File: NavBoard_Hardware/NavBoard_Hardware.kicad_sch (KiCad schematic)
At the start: 45 parts, among them J1 6 Pin Molex Micro-Fit, U1 OKI-5V, U2 BHI160B, U3 ICM-20608-G, U4 OKI-3V3, U6 Raspberry_Pi

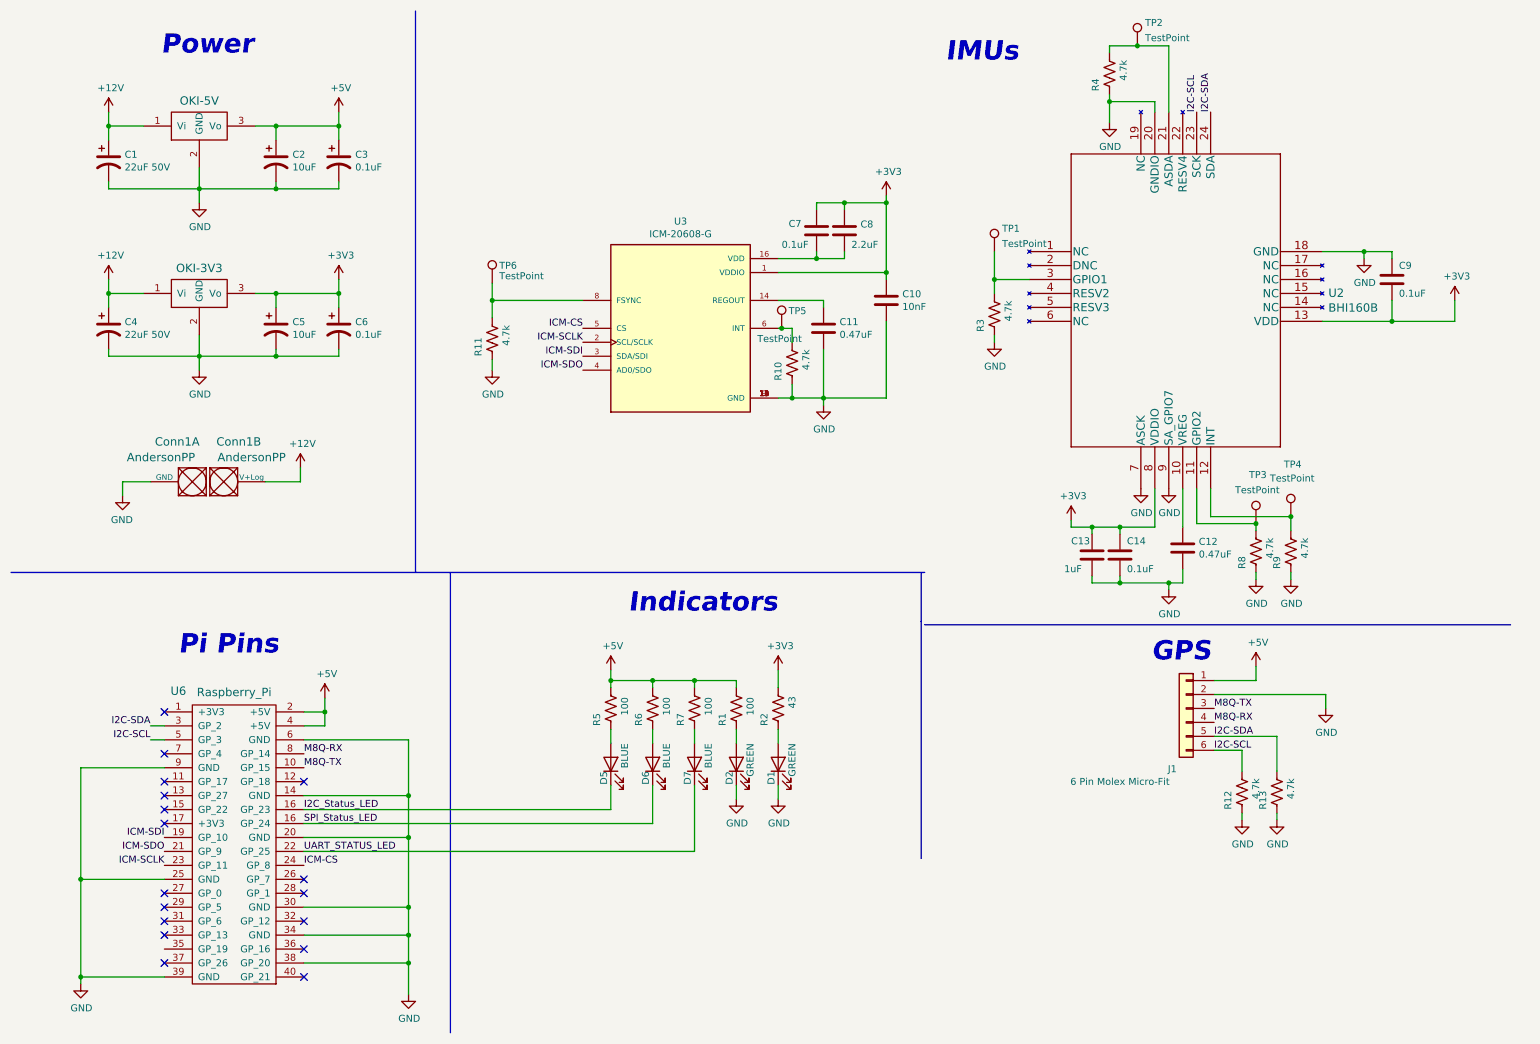
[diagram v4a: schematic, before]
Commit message: Component placement done (except LEDs), redesign of schematic pages, started documentation presentations
Leaving @katdun14 and @nvngx responsible for routing the status LEDs.
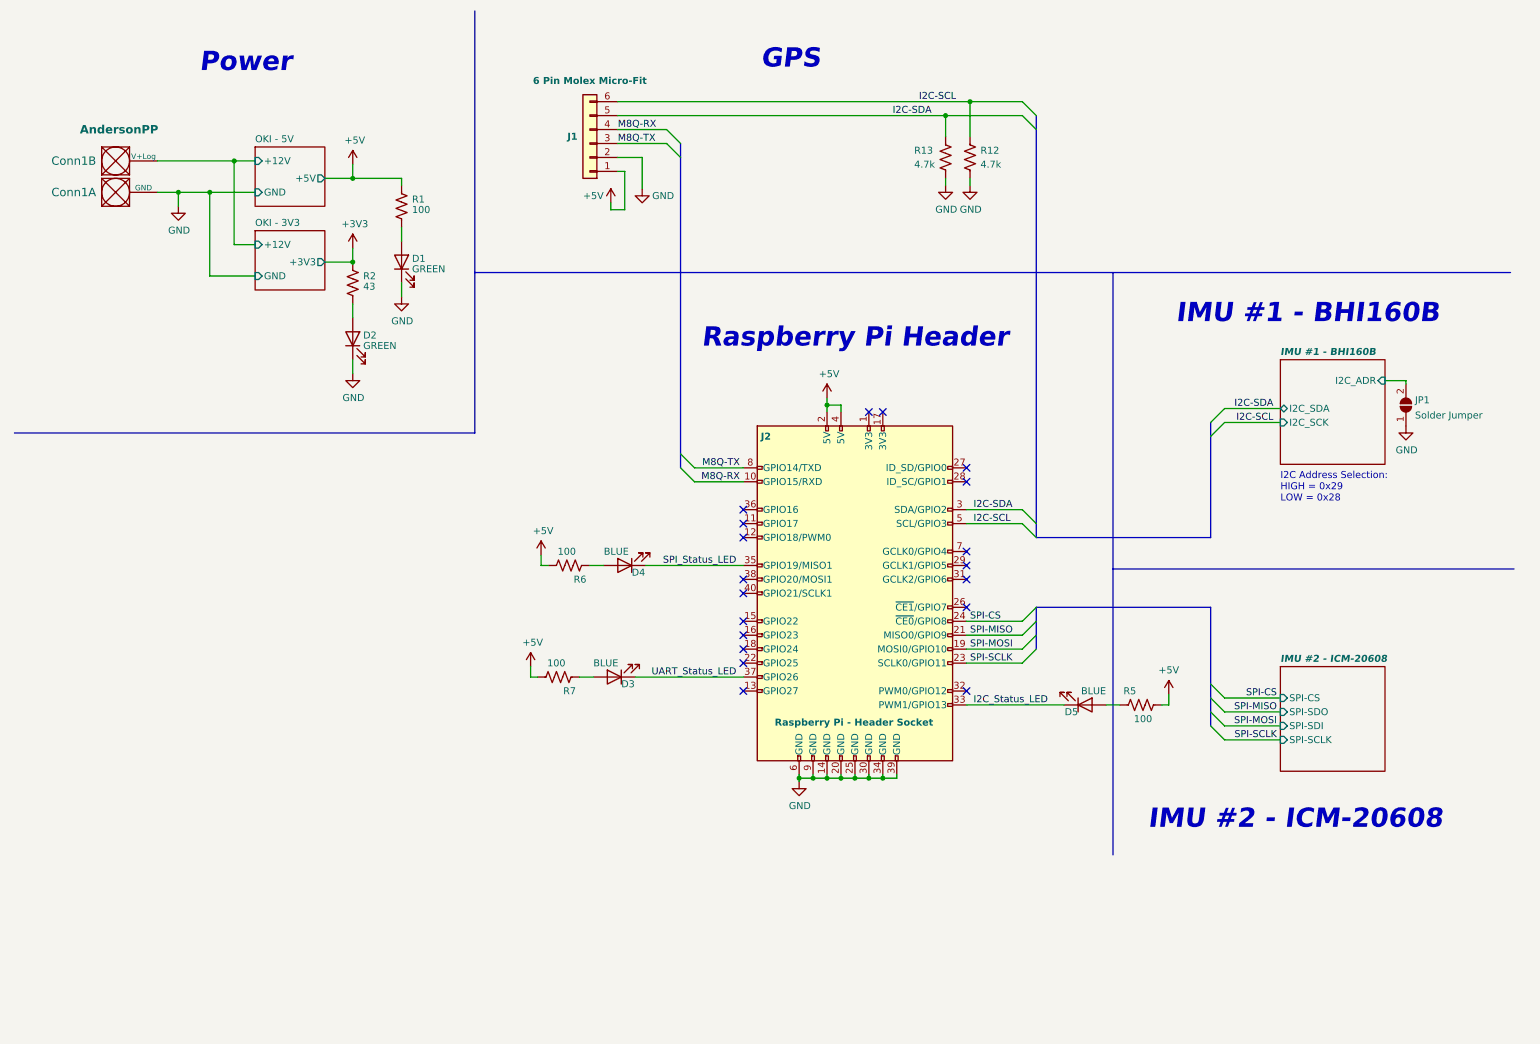
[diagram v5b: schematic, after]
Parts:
- removed C1, C4: 22uF 50V, Capacitor_THT:CP_Radial_D6.3mm_P2.50mm, symbol Device:C_Polarized_US
- removed C10: 10nF, Capacitor_SMD:C_0603_1608Metric_Pad1.08x0.95mm_HandSolder, symbol Device:C
- removed C11, C12: 0.47uF, Capacitor_SMD:C_0603_1608Metric_Pad1.08x0.95mm_HandSolder, symbol Device:C
- removed C13: 1uF, Capacitor_SMD:C_0603_1608Metric_Pad1.08x0.95mm_HandSolder, symbol Device:C
- removed C14, C7, C9: 0.1uF, Capacitor_SMD:C_0603_1608Metric_Pad1.08x0.95mm_HandSolder, symbol Device:C
- removed C2, C5: 10uF, Capacitor_SMD:C_0603_1608Metric_Pad1.08x0.95mm_HandSolder, symbol Device:C_Polarized_US
- removed C3, C6: 0.1uF, Capacitor_SMD:C_0603_1608Metric_Pad1.08x0.95mm_HandSolder, symbol Device:C_Polarized_US
- removed C8: 2.2uF, Capacitor_SMD:C_0603_1608Metric_Pad1.08x0.95mm_HandSolder, symbol Device:C
- removed R10, R11, R3, R4, R8, R9: 4.7k, Resistor_SMD:R_0603_1608Metric_Pad0.98x0.95mm_HandSolder, symbol Device:R_US
- removed TP1, TP2, TP3, TP4, TP5, TP6: TestPoint, TestPoint:TestPoint_Pad_D2.0mm, symbol Connector:TestPoint
- removed U1: OKI-5V, MRDT_Devices:OKI_Horizontal, symbol MRDT_Devices:OKI
- removed U2: BHI160B, LGA24_3X3X0P95_3_BOS, symbol MRDT_Sensors:BHI160B
- removed U3: ICM-20608-G, PQFN50P300X300X80-16N, symbol MRDT_Sensors:ICM-20608-G
- removed U4: OKI-3V3, MRDT_Devices:OKI_Horizontal, symbol MRDT_Devices:OKI
- removed U6: Raspberry_Pi, MRDT_Shields:RaspberryPi_THT_BOTTOM, symbol MRDT_Shields:Raspberry_Pi
- added J2: Raspberry Pi - Header Socket, MRDT_Shields:RaspberryPi_THT_BOTTOM, symbol Connector:Raspberry_Pi_2_3
- added JP1: Solder Jumper, Jumper:SolderJumper-2_P1.3mm_Open_RoundedPad1.0x1.5mm, symbol Jumper:SolderJumper_2_Open
- renumbered D2 to D1, D1 to D2, D7 to D3, D6 to D4
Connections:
- net +5V: now also J2.2 (5V), J2.4 (5V)
- net GND: now also J2.14 (GND), J2.20 (GND), J2.25 (GND), J2.30 (GND), J2.34 (GND), J2.39 (GND), J2.6 (GND), J2.9 (GND), JP1.1 (A)
- net I2C-SCL: now also J2.5 (SCL/GPIO3)
- net I2C-SDA: now also J2.3 (SDA/GPIO2)
- net I2C_Status_LED: now also J2.33 (PWM1/GPIO13)
- net M8Q-RX: now also J2.10 (GPIO15/RXD)
- net M8Q-TX: now also J2.8 (GPIO14/TXD)
- net SPI_Status_LED: now also J2.35 (GPIO19/MISO1)
- net +12V renamed OKI - 3V3/+12V
- net UART_STATUS_LED renamed UART_Status_LED
- net UART_Status_LED: now also J2.37 (GPIO26)
- new net IMU #1 - BHI160B/I2C_ADR: JP1.2 (B)
- new net SPI-CS: J2.24 (~{CE0}/GPIO8)
- new net SPI-MISO: J2.21 (MISO0/GPIO9)
- new net SPI-MOSI: J2.19 (MOSI0/GPIO10)
- new net SPI-SCLK: J2.23 (SCLK0/GPIO11)
- no-connect marks 17 -> 19
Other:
- added sheet IMU #1 - BHI160B (component_sheets\BHI160B.kicad_sch)
- added sheet IMU #2 - ICM-20608 (component_sheets\ICM-20608.kicad_sch)
- added sheet OKI - 3V3 (component_sheets\OKI-3V3.kicad_sch)
- added sheet OKI - 5V (component_sheets\OKI-5V.kicad_sch)
- note added: "I2C Address Selection: HIGH = 0x29 LOW = 0x28"
- note added: "IMU #1 - BHI160B"
- note added: "IMU #2 - ICM-20608"
- note added: "Raspberry Pi Header"
- note removed: "IMUs"
- note removed: "Indicators"
- note removed: "Pi Pins"
- moved on the sheet: Conn1A, Conn1B, D1, D2, D3, D4, D5, J1, R1, R12, R13, R2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

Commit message: Added ground vias for added isolation in substrate, worked on schematic review 1 powerpoint
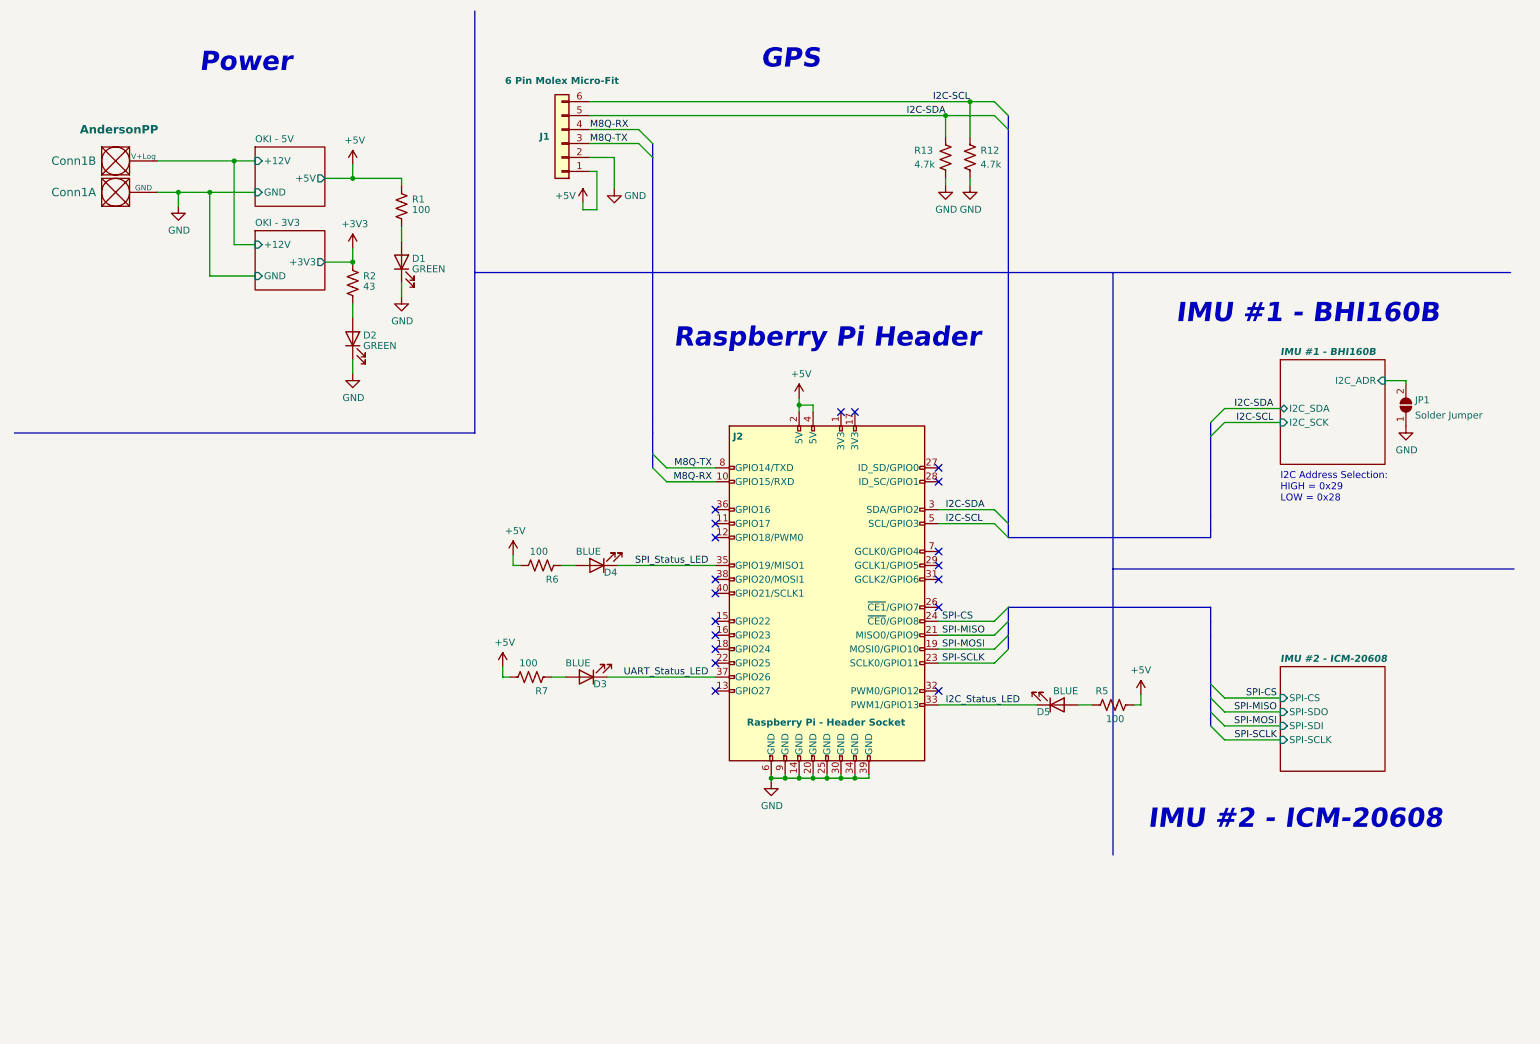
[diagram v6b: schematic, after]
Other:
- moved on the sheet: D3, D4, D5, J1, J2, R5, R6, R7

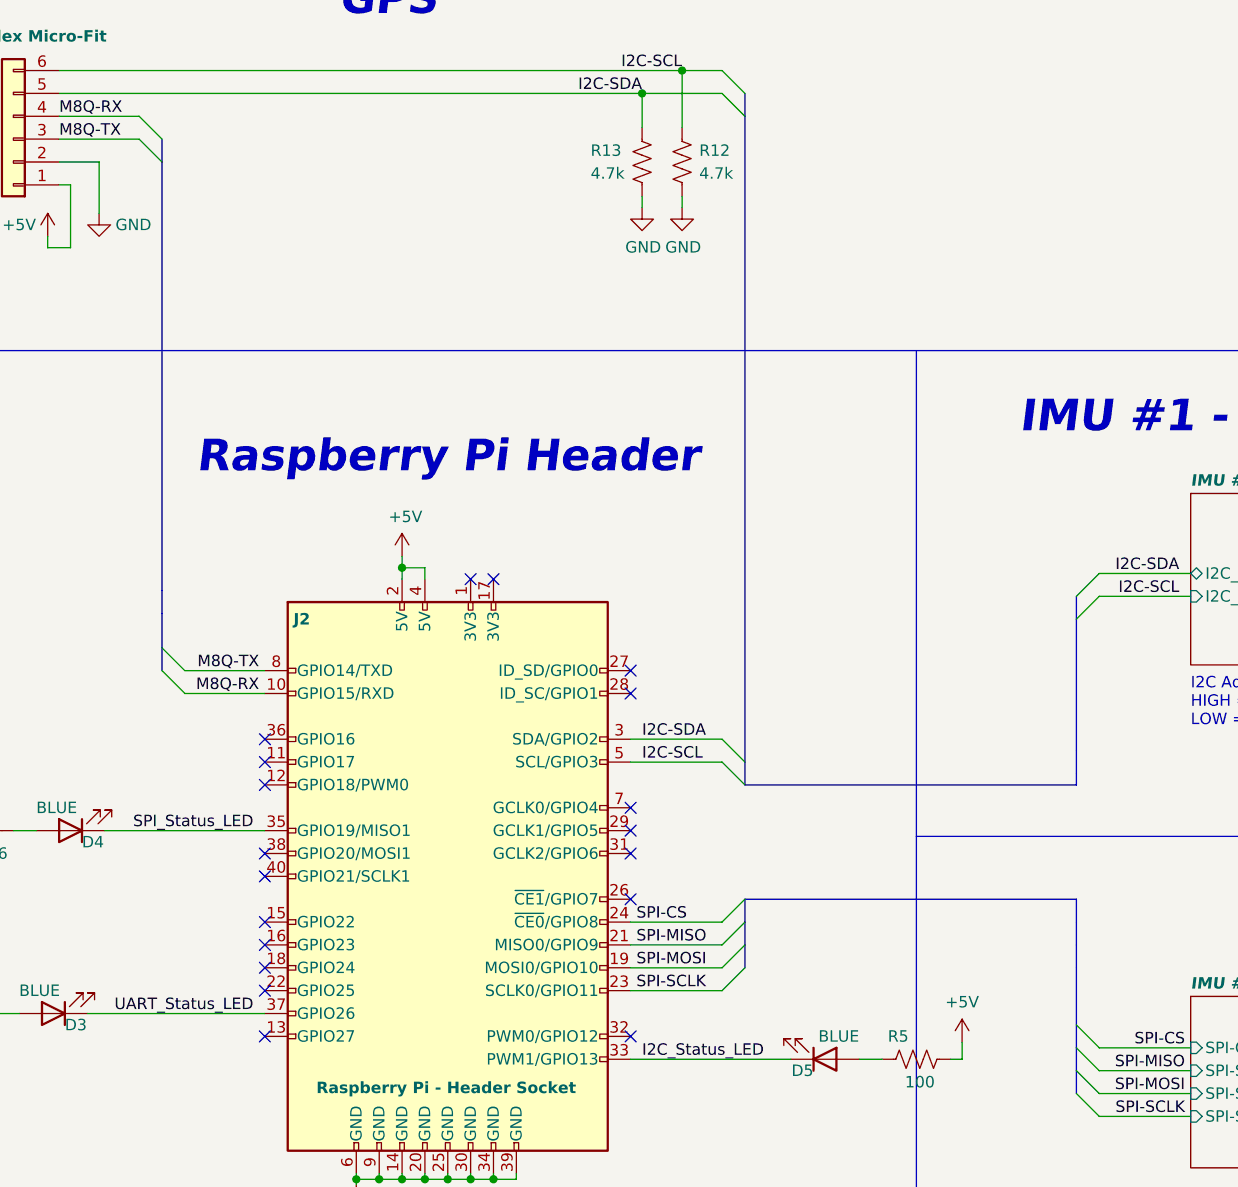
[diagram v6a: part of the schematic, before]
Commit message: Added Information To Voltage Regulator Component Sheets, Improved Schematic Review 1 Powerpoint
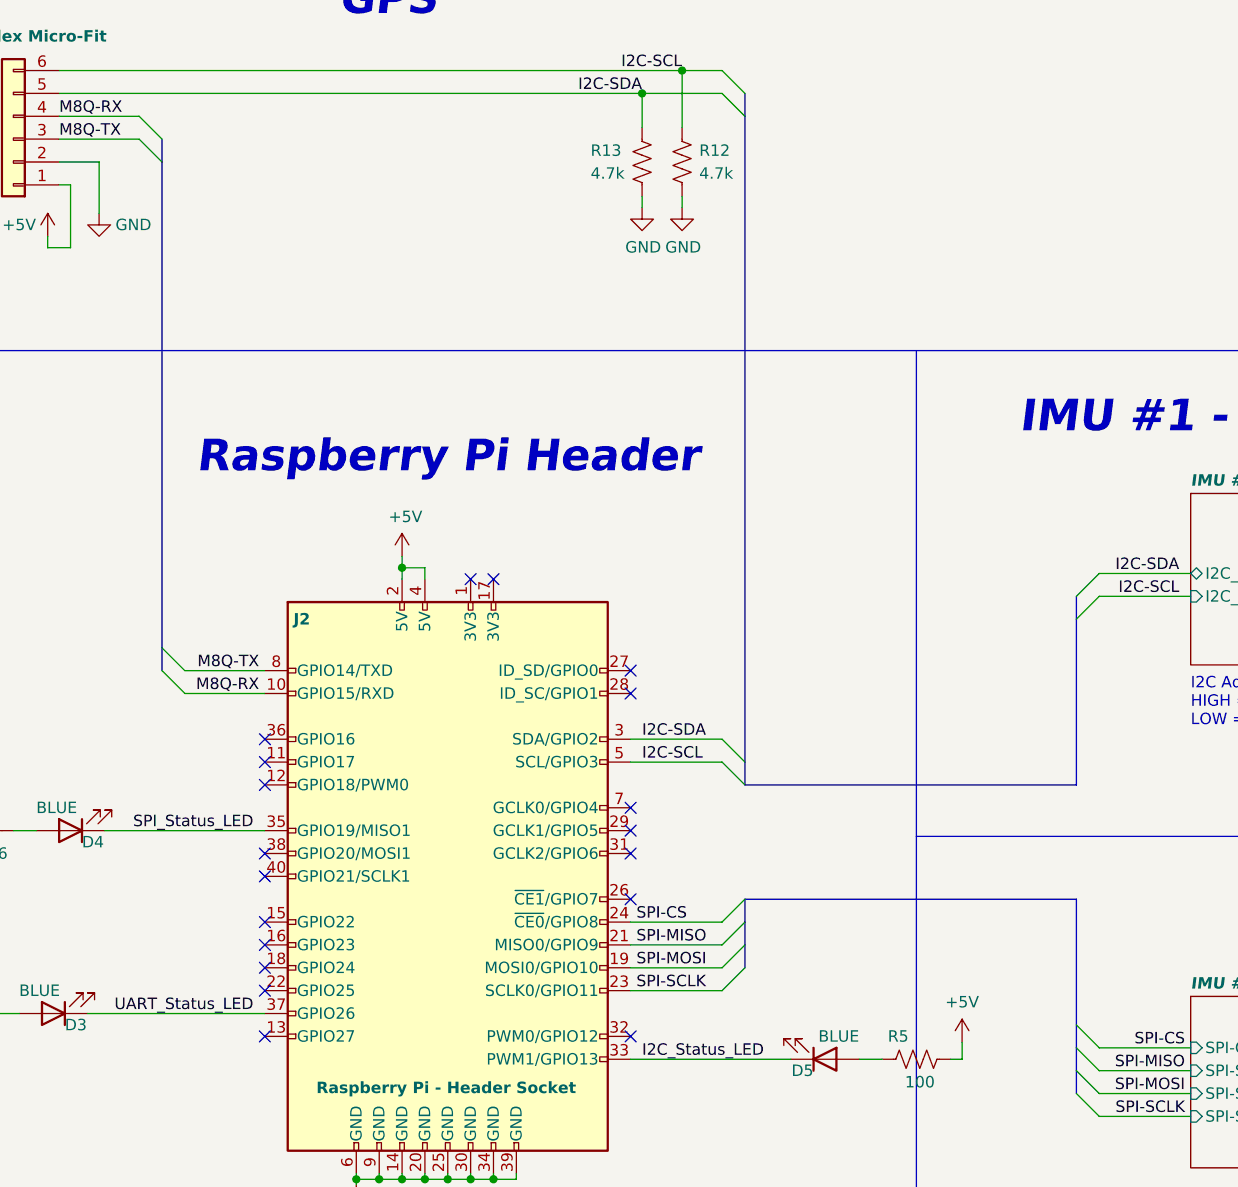
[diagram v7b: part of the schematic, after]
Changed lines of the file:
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@@
-    (stroke (width 0) (type default) (color 0 0 0 0))
-  )
-  (bus (pts (xy 229.87 128.27) (xy 229.87 134.62))
     (stroke (width 0) (type default) (color 0 0 0 0))
   )
@@
     (stroke (width 0) (type default) (color 0 0 0 0))
   )
-  (bus (pts (xy 229.87 104.14) (xy 229.87 106.68))
-    (stroke (width 0) (type default) (color 0 0 0 0))
-  )
   (wire (pts (xy 130.81 95.25) (xy 139.7 95.25))
     (stroke (width 0) (type default) (color 0 0 0 0))
@@
     (stroke (width 0) (type default) (color 0 0 0 0))
   )
-  (bus (pts (xy 128.27 88.9) (xy 128.27 92.71))
-    (stroke (width 0) (type default) (color 0 0 0 0))
-  )
   (wire (pts (xy 38.1 45.085) (xy 41.91 45.085))
     (stroke (width 0) (type default) (color 0 0 0 0))
@@
     (stroke (width 0) (type default) (color 0 0 0 0))
   )
-  (bus (pts (xy 229.87 123.19) (xy 229.87 125.73))
-    (stroke (width 0) (type default) (color 0 0 0 0))
-  )
   (wire (pts (xy 115.57 48.26) (xy 115.57 46.99))
     (stroke (width 0) (type default) (color 0 0 0 0))
@@
     (stroke (width 0) (type default) (color 0 0 0 0))
   )
-  (bus (pts (xy 229.87 125.73) (xy 229.87 128.27))
-    (stroke (width 0) (type default) (color 0 0 0 0))
-  )
   (wire (pts (xy 180.34 125.73) (xy 190.5 125.73))
     (stroke (width 0) (type default) (color 0 0 0 0))
@@
     (stroke (width 0) (type default) (color 0 0 0 0))
   )
-  (bus (pts (xy 229.87 120.65) (xy 229.87 123.19))
+  (bus (pts (xy 229.87 120.65) (xy 229.87 134.62))
     (stroke (width 0) (type default) (color 0 0 0 0))
   )
@@
     (stroke (width 0) (type default) (color 0 0 0 0))
   )
-  (bus (pts (xy 229.87 106.68) (xy 229.87 107.95))
+  (bus (pts (xy 229.87 89.535) (xy 229.87 107.95))
     (stroke (width 0) (type default) (color 0 0 0 0))
   )
@@
     (stroke (width 0) (type default) (color 0 0 0 0))
   )
-  (bus (pts (xy 229.87 89.535) (xy 229.87 104.14))
-    (stroke (width 0) (type default) (color 0 0 0 0))
-  )
   (wire (pts (xy 217.17 136.525) (xy 217.17 138.43))
     (stroke (width 0) (type default) (color 0 0 0 0))
@@
     (stroke (width 0) (type default) (color 0 0 0 0))
   )
-  (bus (pts (xy 128.27 86.36) (xy 128.27 88.9))
-    (stroke (width 0) (type default) (color 0 0 0 0))
-  )
   (wire (pts (xy 242.57 86.995) (xy 232.41 86.995))
     (stroke (width 0) (type default) (color 0 0 0 0))
@@
     (stroke (width 0) (type default) (color 0 0 0 0))
   )
-  (bus (pts (xy 128.27 38.735) (xy 128.27 86.36))
-    (stroke (width 0) (type default) (color 0 0 0 0))
-  )
+  (bus (pts (xy 128.27 38.735) (xy 128.27 92.71))
+    (stroke (width 0) (type default) (color 0 0 0 0))
+  )
